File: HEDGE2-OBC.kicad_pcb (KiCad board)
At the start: 4 copper layers, 90.2 x 95.9 mm, 73 parts, among them J1 SMA-J-P-X-RA-TH1, U1 ADP7158ARDZ-3.3-R7, U10 MAX6633MSA_T, U3 TXS0102QDCURQ1, U4 INA260AIPWR, U5 INA260AIPWR, U6 SN65HVD1782QDRQ1, U7 SN65HVD1782QDRQ1, U8 TCAN1046AVDYYRQ1, U9 MAX6633MSA_T

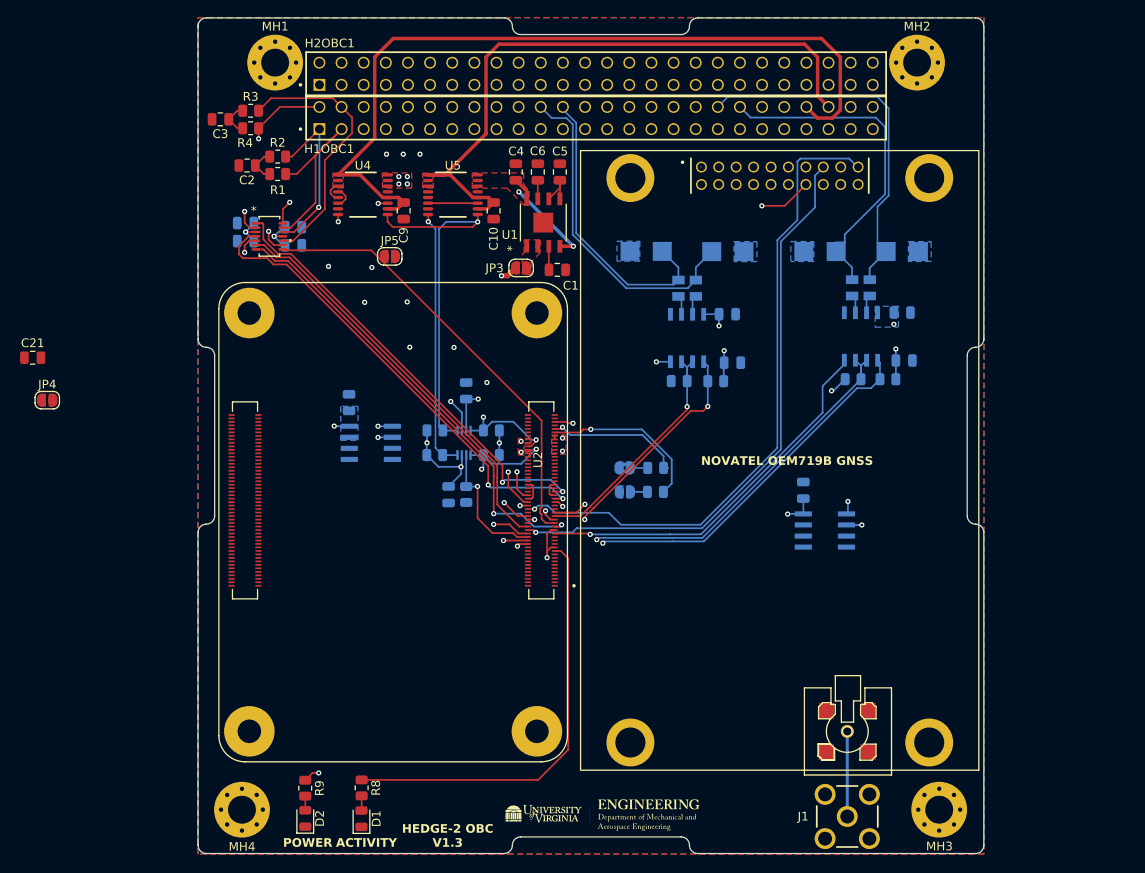
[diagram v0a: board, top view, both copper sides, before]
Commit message: Clean up CM4 routing
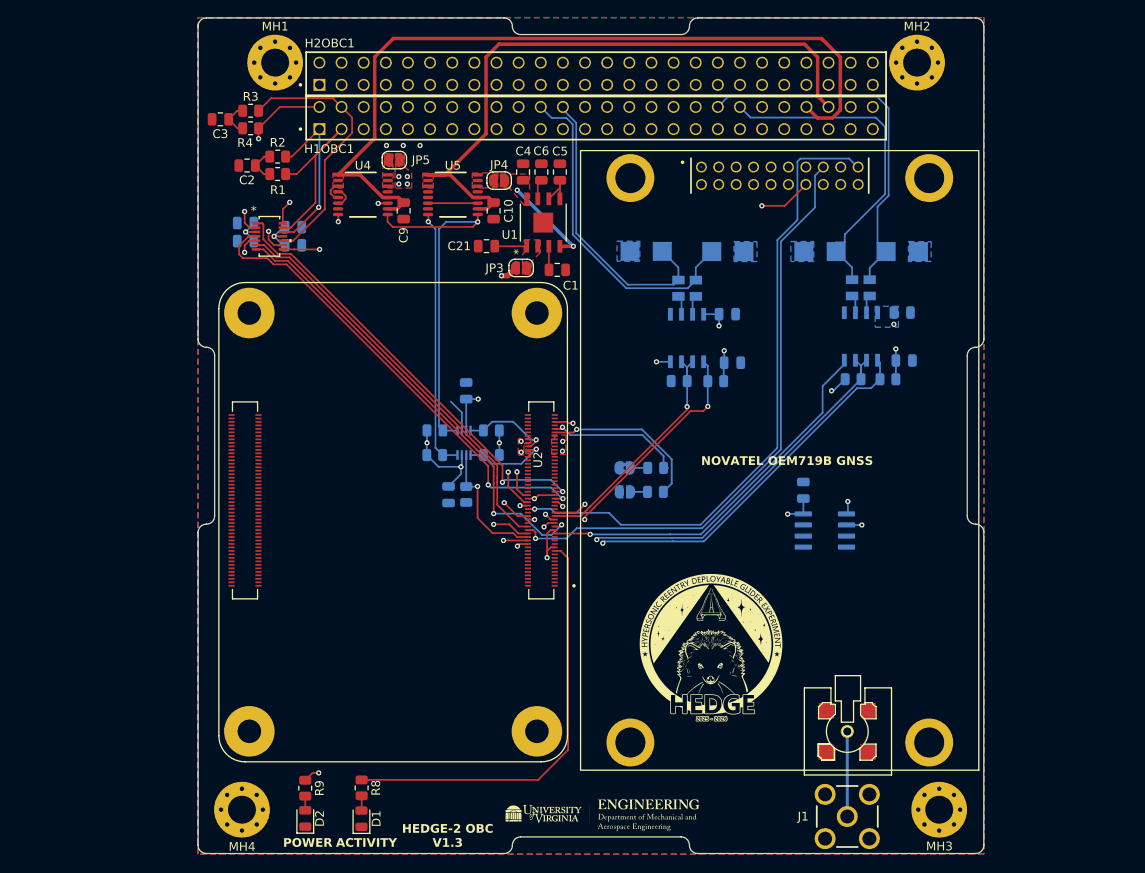
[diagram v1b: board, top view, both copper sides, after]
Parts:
- removed C19: 0u1, Capacitor_SMD:C_0805_2012Metric
- removed U9: MAX6633MSA_T, MAX6635MSA_T:SOIC127P600X175-8N
- G***: moved to F.Cu
- moved JP4 57.6 mm to (198.7, 108.2)
- moved C21 53.6 mm to (197.2, 115.7), turned to 180 degrees
- moved JP5 11.1 mm to (186.6, 105.8), turned to 180 degrees
- moved C4 0.83 mm to (201.4, 107.2)
- moved C6 0.41 mm to (203.5, 107.2)
- turned G*** to 0 degrees
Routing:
- net /SCL0_3V3: track 73.4 -> 56.3 mm, vias 4 -> 2
- net /SDA0_3V3: track 70.0 -> 53.4 mm, vias 4 -> 2
- net Net-(JP3-A): track 0.01 -> 3.69 mm
- net +5V_OEM719B: track 13.0 -> 10.7 mm
- net GND: track 41.9 -> 40.2 mm, vias 19 -> 12
- net +3V3: track 17.5 -> 15.8 mm, vias 7 -> 6
- net /CAN_A_S: track 51.7 -> 52.8 mm
- net /GNSS_RXD2: track 67.4 -> 68.5 mm
- net /CAN_B_RXD: track 52.4 -> 53.2 mm
- net /CAN_B_S: track 50.9 -> 50.6 mm, vias 0 -> 2
- added copper zone on F.Cu, net /INA260_CM4/LOAD
- added copper zone on F.Cu, net /INA260_OEM719/LOAD
- removed copper zone on B.Cu, net +3V3

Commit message: Add PCM5102A I2S audio output for APRS radio
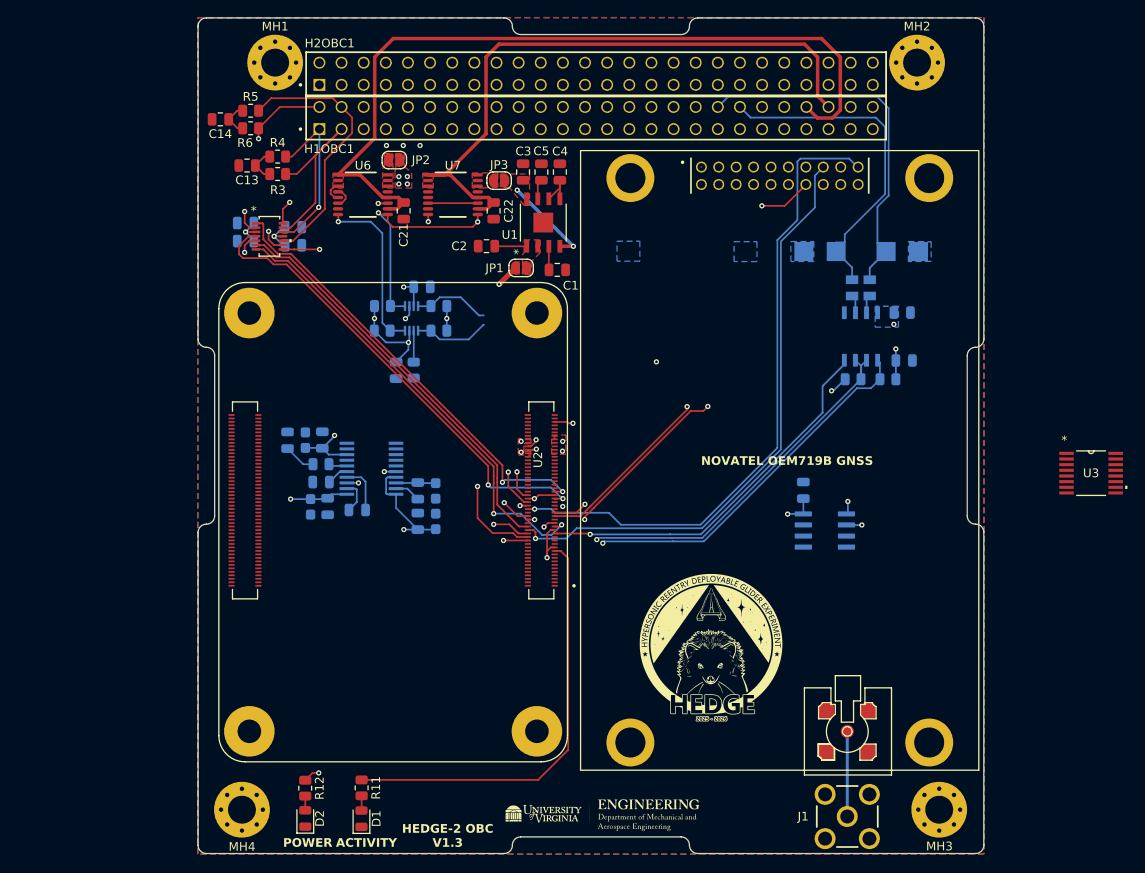
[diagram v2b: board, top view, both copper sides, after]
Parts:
- removed the C13 at (224.8, 123.5)
- removed the C14 at (225.4, 129.1)
- removed CR3, CR4: SMBJ43CA, SMBJ43CA:SMBJSeries_LTF
- removed the JP1 at (213.1, 143.9)
- removed the JP2 at (213.1, 141.2)
- removed the R16 at (223.5, 131.2)
- removed R17: 10k, Resistor_SMD:R_0805_2012Metric
- removed R18, R19: CRGP0805F10R, CRGP0805F10R:RESC2012X65N
- removed the R6 at (216.6, 143.9)
- removed the R7 at (216.6, 141.2)
- removed the U7 at (220.2, 126.3)
- added C10: 2u2, Capacitor_SMD:C_0805_2012Metric, B.Cu at (182.4, 146.0)
- added C11: 0u1, Capacitor_SMD:C_0805_2012Metric, B.Cu at (179.0, 145.6)
- added C12: 0u1, Capacitor_SMD:C_0805_2012Metric, B.Cu at (178.4, 138.0)
- added C17: 10u, Capacitor_Tantalum_SMD:CP_EIA-2012-12_Kemet-R, B.Cu at (191.4, 147.3)
- added C18: 0u1, Capacitor_SMD:C_0805_2012Metric, B.Cu at (189.3, 147.3)
- added C19: 0u1, Capacitor_SMD:C_0805_2012Metric, B.Cu at (189.3, 143.8)
- added C20: 10u, Capacitor_Tantalum_SMD:CP_EIA-2012-12_Kemet-R, B.Cu at (191.4, 143.8)
- added C6: 2n2, Capacitor_SMD:C_0805_2012Metric, B.Cu at (174.4, 138.0)
- added C7: 2u2, Capacitor_SMD:C_0805_2012Metric, B.Cu at (178.2, 142.8)
- added C8: 10u, Capacitor_Tantalum_SMD:CP_EIA-2012-12_Kemet-R, B.Cu at (177.0, 145.6)
- added C9: 10u, Capacitor_Tantalum_SMD:CP_EIA-2012-12_Kemet-R, B.Cu at (176.4, 138.0)
- added G***: LOGO, HEDGElogo:HEDGE-logo, B.Cu at (210.5, 181.0)
- added G***: LOGO, HEDGE:HEDGE2-logo, B.Cu at (187.0, 161.8)
- added R1: 470, Resistor_SMD:R_0805_2012Metric, B.Cu at (178.2, 140.8)
- added U3: SN74CBTLV3257PWR, SN74CBTLV3257PWR:PW16, F.Cu at (266.6, 141.8)
- added U4: PCM5102AQPWRQ1, PCM5102AQPWRQ1:PW20, B.Cu at (184.0, 141.3)
- moved U5 15.5 mm to (188.6, 124.0)
- moved C16 15.5 mm to (186.8, 130.0)
- moved R2 15.5 mm to (188.8, 129.9)
- moved R7 15.5 mm to (185.3, 122.6)
- moved R10 15.5 mm to (191.7, 122.6)
- moved R8 15.5 mm to (185.2, 125.4)
- moved R9 15.5 mm to (191.7, 125.4)
- moved C15 13.0 mm to (189.8, 120.4), turned to 180 degrees
- renumbered C2 to C13, C3 to C14, C7 to C15, C8 to C16, C21 to C2, C9 to C21, C10 to C22, C11 to C23, C12 to C24, C15 to C27, C16 to C28, C17 to C29, C4 to C3, C18 to C30, C20 to C31, C5 to C4, C6 to C5, JP3 to JP1, JP5 to JP2, JP4 to JP3, R11 to R10, R8 to R11, R9 to R12, R12 to R13, R13 to R14, R14 to R15, R15 to R16, R5 to R2, R1 to R3, R2 to R4, R3 to R5, R4 to R6, R20 to R7, R21 to R8, R10 to R9, U8 to U10, U10 to U11, U3 to U5, U4 to U6, U5 to U7, U6 to U8
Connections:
- net +3V3 renamed +3V3<CM4
- net +3V3_OEM719B renamed +3V3>OEM719B
- H1OBC1 pad 05: /UART_A_TX -> unconnected-(H1OBC1-Pad05)
- H1OBC1 pad 06: /UART_B_TX -> unconnected-(H1OBC1-Pad06)
- H1OBC1 pad 07: /UART_A_RX -> unconnected-(H1OBC1-Pad07)
- H1OBC1 pad 08: /UART_B_RX -> unconnected-(H1OBC1-Pad08)
- H1OBC1 pad 13: /UART_C_TX -> unconnected-(H1OBC1-Pad13)
- H1OBC1 pad 15: /UART_C_RX -> unconnected-(H1OBC1-Pad15)
- H1OBC1 pad 22: /UART_D_TX -> unconnected-(H1OBC1-Pad22)
- H1OBC1 pad 24: /UART_D_RX -> unconnected-(H1OBC1-Pad24)
- H1OBC1 pad 25: /5V_PERM -> unconnected-(H1OBC1-Pad25)
- H1OBC1 pad 26: /5V_PERM -> unconnected-(H1OBC1-Pad26)
- H1OBC1 pad 45: /ENA_PWR_1 -> unconnected-(H1OBC1-Pad45)
- H1OBC1 pad 47: /ENA_PWR_2 -> unconnected-(H1OBC1-Pad47)
- H1OBC1 pad 49: /ENA_PWR_3 -> unconnected-(H1OBC1-Pad49)
- H1OBC1 pad 50: /PWR_3 -> unconnected-(H1OBC1-Pad50)
- H1OBC1 pad 51: /ENA_PWR_4 -> unconnected-(H1OBC1-Pad51)
- H1OBC1 pad 52: /PWR_4 -> unconnected-(H1OBC1-Pad52)
- H2OBC1 pad 01: unconnected-(H2OBC1-Pad01) -> /DIN/CONFIG/DIO14_XB
- H2OBC1 pad 02: unconnected-(H2OBC1-Pad02) -> /DOUT/DIO13_XB
- H2OBC1 pad 03: unconnected-(H2OBC1-Pad03) -> /RTS/DIO6_XB
- H2OBC1 pad 04: unconnected-(H2OBC1-Pad04) -> /CTS/DIO7_XB
- H2OBC1 pad 05: unconnected-(H2OBC1-Pad05) -> /AD3/DIO3/SPI_SSEL_XB
- H2OBC1 pad 06: unconnected-(H2OBC1-Pad06) -> /AD2/DIO2/SPI_CLK_XB
- H2OBC1 pad 07: unconnected-(H2OBC1-Pad07) -> /DIO4/SPI_MOSI_XB
- H2OBC1 pad 08: unconnected-(H2OBC1-Pad08) -> /DIO12/SPI_MISO_XB
- H2OBC1 pad 09: unconnected-(H2OBC1-Pad09) -> /DTR/SLEEP_RQ/DIO8_XB
- H2OBC1 pad 10: unconnected-(H2OBC1-Pad10) -> /AD1/DIO1/SPI_ATTN_XB
- H2OBC1 pad 11: unconnected-(H2OBC1-Pad11) -> /ON_SLEEP/DIO9_XB
- H2OBC1 pad 12: unconnected-(H2OBC1-Pad12) -> /DIO10/PWM0_XB
- H2OBC1 pad 13: unconnected-(H2OBC1-Pad13) -> /RESET_XB
- H2OBC1 pad 14: unconnected-(H2OBC1-Pad14) -> /DIO11/PWM1_XB
- H2OBC1 pad 15: unconnected-(H2OBC1-Pad15) -> /AD0/DIO0_XB
- H2OBC1 pad 16: unconnected-(H2OBC1-Pad16) -> /Associate/DIO5_XB
- H2OBC1 pad 17: unconnected-(H2OBC1-Pad17) -> /NDTR_XB
- H2OBC1 pad 19: unconnected-(H2OBC1-Pad19) -> /MIC_IN_DMR
- H2OBC1 pad 20: unconnected-(H2OBC1-Pad20) -> /LINE_OUT_DMR
- H2OBC1 pad 21: unconnected-(H2OBC1-Pad21) -> /T/R_DMR
- H2OBC1 pad 22: unconnected-(H2OBC1-Pad22) -> /PTT_DMR
- H2OBC1 pad 23: unconnected-(H2OBC1-Pad23) -> /SPKEN_DMR
- H2OBC1 pad 24: unconnected-(H2OBC1-Pad24) -> /CS_DMR
- H2OBC1 pad 25: /5V_PERM -> /HST_RXD_DMR
- H2OBC1 pad 26: /5V_PERM -> /UART_RX_DMR
- H2OBC1 pad 27: unconnected-(H2OBC1-Pad27) -> /HST_TXD_DMR
- H2OBC1 pad 28: unconnected-(H2OBC1-Pad28) -> /UART_TX_DMR
- H2OBC1 pad 41: unconnected-(H2OBC1-Pad41) -> /BATT
- H2OBC1 pad 42: unconnected-(H2OBC1-Pad42) -> /BATT
- H2OBC1 pad 43: unconnected-(H2OBC1-Pad43) -> /BATT
- H2OBC1 pad 44: unconnected-(H2OBC1-Pad44) -> /BATT
- H2OBC1 pad 47: /RBF_C -> unconnected-(H2OBC1-Pad47)
- H2OBC1 pad 48: /DS_C -> unconnected-(H2OBC1-Pad48)
- H2OBC1 pad 49: /RBF_A -> unconnected-(H2OBC1-Pad49)
- H2OBC1 pad 50: /RBF_B -> unconnected-(H2OBC1-Pad50)
- H2OBC1 pad 51: /DS_A -> unconnected-(H2OBC1-Pad51)
- H2OBC1 pad 52: /DS_B -> unconnected-(H2OBC1-Pad52)
- Module1 pad 24: unconnected-(Module1A-GPIO26-Pad24) -> /UART_SCI_DIR
- Module1 pad 25: unconnected-(Module1A-GPIO21-Pad25) -> /PCM_DOUT
- Module1 pad 26: /UART_SCI_DIR -> /PCM_FS
- Module1 pad 39: /UART_COMM_A -> /UART_TX_DMR
- Module1 pad 40: /UART_COMM_B -> /UART_RX_DMR
- Module1 pad 41: /UART_COMM_DIR -> /PTT_DMR
- Module1 pad 47: unconnected-(Module1A-GPIO23-Pad47) -> /CAN_A_S
- Module1 pad 49: /CAN_A_S -> /PCM_CLK
- Module1 pad 89: Net-(Module1A-WiFi_nDisable) -> unconnected-(Module1A-WiFi_nDisable-Pad89)
- Module1 pad 91: Net-(Module1A-BT_nDisable) -> unconnected-(Module1A-BT_nDisable-Pad91)
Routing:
- net /UART_D_TX: track 38.2 -> 0.00 mm
- net /UART_D_RX: track 35.0 -> 0.00 mm
- net /UART_COMM_B: track 31.5 -> 0.00 mm, vias 3 -> 0
- net /UART_COMM_DIR: track 28.5 -> 0.00 mm, vias 1 -> 0
- net /UART_COMM_A: track 26.8 -> 0.00 mm, vias 2 -> 0
- net /UART_RX_DMR: track 0.00 -> 26.2 mm, vias 0 -> 3
- net +3V3<CM4: track 15.8 -> 40.8 mm, vias 6 -> 9
- net /PTT_DMR: track 0.00 -> 20.6 mm, vias 0 -> 1
- net Net-(Module1A-WiFi_nDisable): track 19.0 -> 0.00 mm, vias 1 -> 0
- net Net-(Module1A-BT_nDisable): track 15.8 -> 0.00 mm, vias 1 -> 0
- net /SCL0_5V: track 42.3 -> 26.6 mm, vias 1 -> 2
- net /UART_SCI_DIR: track 53.5 -> 42.8 mm, vias 2 -> 1
- net /SDA0_5V: track 41.7 -> 31.4 mm
- net +5V_CM4: track 26.1 -> 19.5 mm, vias 13 -> 11
- net Net-(U4-CAPM): track 0.00 -> 5.60 mm
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
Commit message: Add PCM and SPI UART; begin layout update
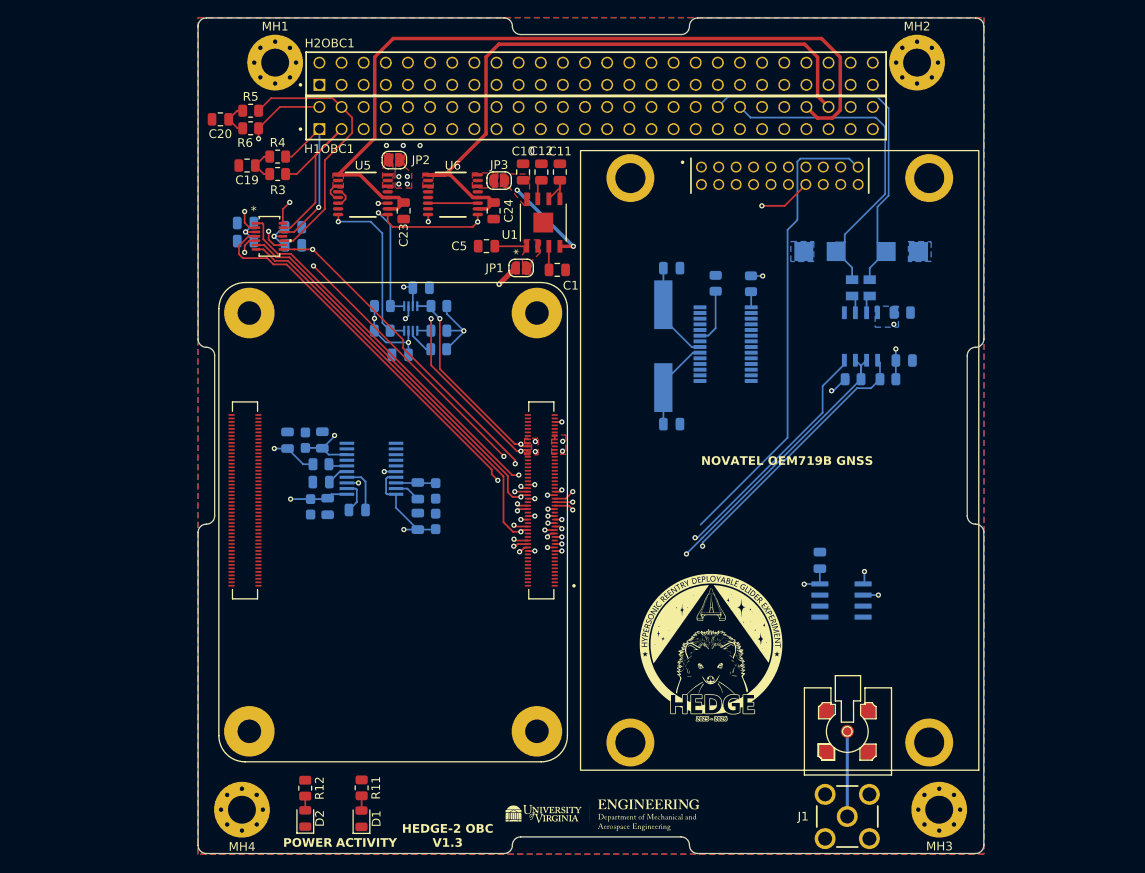
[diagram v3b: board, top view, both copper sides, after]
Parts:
- removed the U3 at (266.6, 141.8)
- added C17: 36p, Capacitor_SMD:C_0805_2012Metric, B.Cu at (218.4, 136.2)
- added C18: 36p, Capacitor_SMD:C_0805_2012Metric, B.Cu at (218.4, 118.2)
- added IC1: SC16IS752IPW, SC16IS752IPW:SOP65P640X110-28N, B.Cu at (224.6, 127.0)
- added R17: 1k, Resistor_SMD:R_0805_2012Metric, B.Cu at (227.6, 120.0)
- added R18: 1k, Resistor_SMD:R_0805_2012Metric, B.Cu at (223.5, 120.0)
- added Y1: ABLS-LR-3.072MHZ-T, ABLS-LR-3.072MHZ-T:XTAL_ABLS-LR-3.072MHZ-T, B.Cu at (217.5, 127.2)
- moved U9 8.26 mm to (237.9, 156.4)
- moved C31 8.26 mm to (235.5, 151.8)
- moved R2 3.74 mm to (191.7, 127.5), turned to 180 degrees
- moved C22 1.84 mm to (187.3, 128.2), turned to 180 degrees
- moved C21 0.14 mm to (189.7, 120.5)
- moved U4 0.10 mm to (188.5, 124.0)
- renumbered C3 to C10, C4 to C11, C5 to C12, C17 to C13, C18 to C14, C19 to C15, C20 to C16, C13 to C19, C7 to C2, C14 to C20, C15 to C21, C16 to C22, C21 to C23, C22 to C24, C23 to C25, C24 to C26, C8 to C3, C9 to C4, C2 to C5, C10 to C6, C11 to C7, C12 to C8, C6 to C9, U4 to U2, U2 to U3, U5 to U4, U6 to U5, U7 to U6, U8 to U7, U10 to U8, U11 to U9
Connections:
- net /Antenna renamed Net-(U3-ANT)
- H2OBC1 pad 03: /RTS/DIO6_XB -> unconnected-(H2OBC1-Pad03)
- H2OBC1 pad 04: /CTS/DIO7_XB -> unconnected-(H2OBC1-Pad04)
- H2OBC1 pad 05: /AD3/DIO3/SPI_SSEL_XB -> unconnected-(H2OBC1-Pad05)
- H2OBC1 pad 06: /AD2/DIO2/SPI_CLK_XB -> unconnected-(H2OBC1-Pad06)
- H2OBC1 pad 07: /DIO4/SPI_MOSI_XB -> unconnected-(H2OBC1-Pad07)
- H2OBC1 pad 08: /DIO12/SPI_MISO_XB -> unconnected-(H2OBC1-Pad08)
- H2OBC1 pad 10: /AD1/DIO1/SPI_ATTN_XB -> unconnected-(H2OBC1-Pad10)
- H2OBC1 pad 12: /DIO10/PWM0_XB -> unconnected-(H2OBC1-Pad12)
- H2OBC1 pad 14: /DIO11/PWM1_XB -> unconnected-(H2OBC1-Pad14)
- H2OBC1 pad 15: /AD0/DIO0_XB -> unconnected-(H2OBC1-Pad15)
- H2OBC1 pad 17: /NDTR_XB -> unconnected-(H2OBC1-Pad17)
- H2OBC1 pad 20: /LINE_OUT_DMR -> unconnected-(H2OBC1-Pad20)
- H2OBC1 pad 23: /SPKEN_DMR -> unconnected-(H2OBC1-Pad23)
- H2OBC1 pad 24: /CS_DMR -> unconnected-(H2OBC1-Pad24)
- H2OBC1 pad 25: /HST_RXD_DMR -> unconnected-(H2OBC1-Pad25)
- H2OBC1 pad 27: /HST_TXD_DMR -> unconnected-(H2OBC1-Pad27)
- Module1 pad 29: unconnected-(Module1A-GPIO16-Pad29) -> /SPI3_RESET
- Module1 pad 30: /I2C_EN -> unconnected-(Module1A-GPIO6-Pad30)
- Module1 pad 34: /GNSS_RXD2 -> /CAN_B_RXD
- Module1 pad 35: /CAN_B_RXD -> /SPI3_MISO
- Module1 pad 36: /CAN_B_TXD -> /SPI3_CE0_0
- Module1 pad 39: /UART_TX_DMR -> /DIN/CONFIG/DIO14_XB
- Module1 pad 40: /UART_RX_DMR -> /DOUT/DIO13_XB
- Module1 pad 41: /PTT_DMR -> /Associate/DIO5_XB
- Module1 pad 45: unconnected-(Module1A-GPIO24-Pad45) -> /DTR/SLEEP_RQ/DIO8_XB
- Module1 pad 46: /GNSS_PPS -> /ON_SLEEP/DIO9_XB
- Module1 pad 48: /GNSS_NRESET_IN -> /RESET_XB
- Module1 pad 50: /GNSS_PV -> unconnected-(Module1A-GPIO17-Pad50)
- Module1 pad 54: /GNSS_TXD2 -> /CAN_B_TXD
- Module1 pad 56: unconnected-(Module1A-GPIO3-Pad56) -> /SPI3_SCLK
- Module1 pad 58: unconnected-(Module1A-GPIO2-Pad58) -> /SPI3_MOSI
- R2 pad 1: GND -> +3V3<CM4
- R2 pad 2: /I2C_EN -> Net-(U4-OE)
- U3 pad 26: (no net) -> GND
- U4 pad 6: /I2C_EN -> Net-(U4-OE)
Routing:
- net /nPWR_LED: track 71.5 -> 0.82 mm, vias 2 -> 1
- net /GNSS_RXD2: track 68.5 -> 0.00 mm, vias 1 -> 0
- net /GNSS_PV: track 59.9 -> 0.00 mm, vias 1 -> 0
- net /MIC_IN_DMR: track 3.67 -> 58.5 mm, vias 0 -> 1
- net /GNSS_NRESET_IN: track 51.4 -> 0.00 mm, vias 1 -> 0
- net /PI_nLED_Activity: track 49.0 -> 0.82 mm, vias 0 -> 1
- net /GNSS_TXD2: track 52.5 -> 6.03 mm, vias 2 -> 1
- net /UART_RX_DMR: track 26.2 -> 0.00 mm, vias 3 -> 0
- net /PTT_DMR: track 20.6 -> 0.00 mm, vias 1 -> 0
- net /GNSS_PPS: track 74.4 -> 53.8 mm, vias 1 -> 0
- net /SCL0_3V3: track 56.3 -> 75.2 mm, vias 2 -> 3
- net /SDA0_3V3: track 53.4 -> 71.9 mm, vias 2 -> 3
- net GND: track 43.6 -> 29.3 mm, vias 15 -> 17
- net /I2C_EN: track 13.9 -> 0.00 mm, vias 1 -> 0
- net /UART_SCI_DIR: track 42.8 -> 54.8 mm, vias 1 -> 2
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
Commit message: Continue layout update
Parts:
- removed the C17 at (218.4, 136.2)
- removed the C18 at (218.4, 118.2)
- removed Y1: ABLS-LR-3.072MHZ-T, ABLS-LR-3.072MHZ-T:XTAL_ABLS-LR-3.072MHZ-T
- added C21: 10p, Capacitor_SMD:C_0805_2012Metric, B.Cu at (211.4, 130.1)
- added X1: XLH536003.072000I, XLH53xxxxxx:SON6_XLH5_5p0x3p2-1p27_REN_REN, B.Cu at (215.1, 126.7)
- renumbered C19 to C17, C20 to C18, C21 to C19, C22 to C20, C23 to C22, C24 to C23, C25 to C24, C26 to C25, C27 to C26, C28 to C27, C29 to C28, C30 to C29, C31 to C30, R18 to R11, R17 to R12, R11 to R13, R12 to R14, R13 to R15, R14 to R16, R15 to R17, R16 to R18
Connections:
- IC1 pad 7: Net-(IC1-XTAL2) -> unconnected-(IC1-XTAL2-Pad7)
- Module1 pad 41: /Associate/DIO5_XB -> unconnected-(Module1A-GPIO25-Pad41)
- Module1 pad SH1: (no net) -> GND
- Module1 pad SH2: (no net) -> GND
- Module1 pad SH3: (no net) -> GND
- Module1 pad SH4: (no net) -> GND
- U3 pad 26: GND -> (no net)
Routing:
- net /nPWR_LED: track 0.82 -> 60.1 mm, vias 1 -> 2
- net /SPI3_MOSI: track 0.88 -> 55.2 mm, vias 1 -> 3
- net /Associate/DIO5_XB: track 0.79 -> 51.1 mm, vias 1 -> 2
- net /PTT_DMR: track 0.00 -> 47.8 mm, vias 0 -> 1
- net /T/R_DMR: track 0.00 -> 46.1 mm, vias 0 -> 1
- net /UART_TX_DMR: track 0.00 -> 44.2 mm, vias 0 -> 1
- net /UART_RX_DMR: track 0.00 -> 43.8 mm, vias 0 -> 1
- net /SPI3_SCLK: track 1.50 -> 40.7 mm, vias 1 -> 3
- net /SPI3_CE0_0: track 1.66 -> 39.1 mm, vias 1 -> 4
- net /PI_nLED_Activity: track 0.82 -> 36.6 mm, vias 1 -> 2
- net /GNSS_RXD2: track 0.00 -> 32.3 mm, vias 0 -> 1
- net /SPI3_MISO: track 0.92 -> 32.8 mm, vias 1 -> 2
- net /SPI3_RESET: track 0.82 -> 29.0 mm, vias 1 -> 2
- net /PCM_DOUT: track 0.82 -> 27.3 mm
- net /GNSS_PPS: track 53.8 -> 28.6 mm
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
